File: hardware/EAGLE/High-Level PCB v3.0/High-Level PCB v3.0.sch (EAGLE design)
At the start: 38 parts, among them IC1 DS8921, IC2 DS8921, IC3 MCP2551, J1 Micro-SD, J2 Gyro, J3 Compass, J4 GPS, J5 DB9 Plug, J6 Compass, X1 RJ45, X2 Vehicle control, X4 RJ45

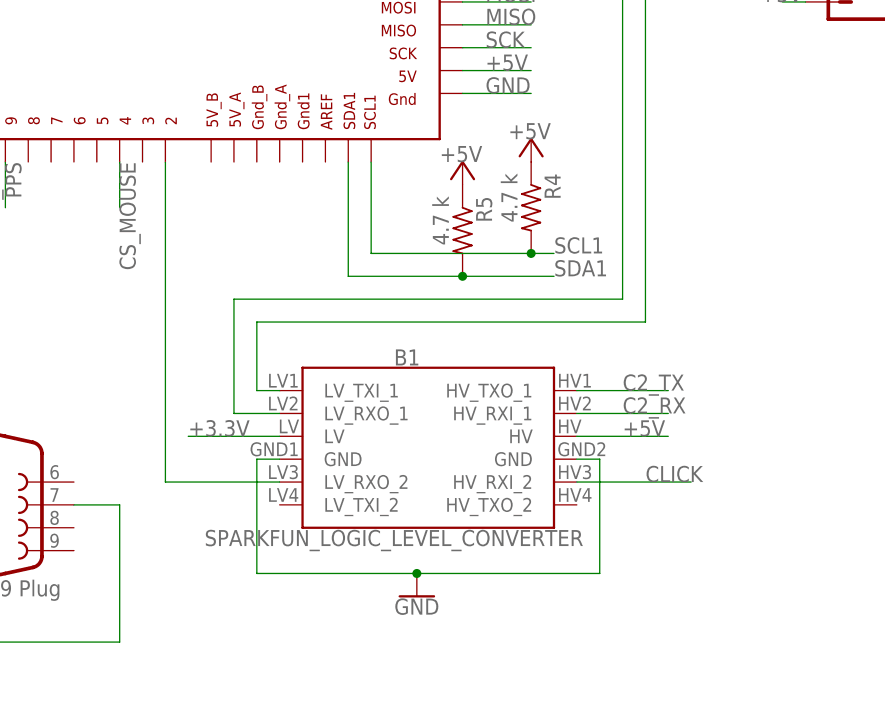
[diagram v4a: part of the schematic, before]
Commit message: Voltage level shifter adafruit
Removed Sparkfun voltage level shifter and replaced with adafruit's
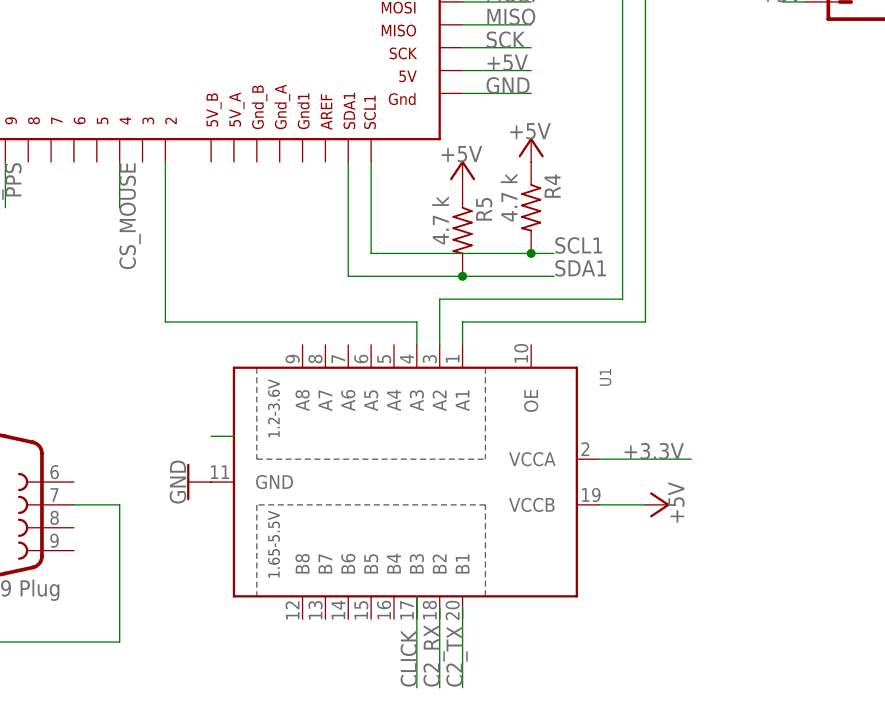
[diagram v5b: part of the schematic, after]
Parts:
- removed B1: SPARKFUN_LOGIC_LEVEL_CONVERTER, SparkFun-Boards:SPARKFUN_LOGIC_LEVEL_CONVERTER
- added U1: (no value), TXb0108:TXB0108PWR
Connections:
- net +3.3V: now also U1.VCCA; no longer B1.LV
- net +5V: now also U1.VCCB; no longer B1.HV
- net C2_RX: no longer B1.HV_RXI_1
- net C2_TX: no longer B1.HV_TXO_1
- net CLICK: no longer B1.HV_RXI_2
- net GND: now also U1.GND; no longer B1.GND, B1.GND@2
- net N$12: now also U1.A3; no longer B1.LV_RXO_2
- net N$4: now also U1.A1; no longer B1.LV_TXI_1
- net N$5: now also U1.A2; no longer B1.LV_RXO_1
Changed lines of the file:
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@@
 <part name="P+2" library="supply1" library_urn="urn:adsk.eagle:library:371" deviceset="+5V" device=""/>
 <part name="P+3" library="supply1" library_urn="urn:adsk.eagle:library:371" deviceset="+5V" device=""/>
-<part name="B1" library="SparkFun-Boards" deviceset="SPARKFUN_LOGIC_LEVEL_CONVERTER" device=""/>
 <part name="GND7" library="SparkFun-PowerSymbols" deviceset="GND" device=""/>
 <part name="S2" library="switch" library_urn="urn:adsk.eagle:library:380" deviceset="255SB" device="" package3d_urn="urn:adsk.eagle:package:27679/1" value="Click Source"/>
@@
 <part name="J7" library="SparkFun-Connectors" deviceset="CONN_03" device="-SCREW-5MM"/>
 <part name="GND11" library="SparkFun-PowerSymbols" deviceset="GND" device=""/>
+<part name="U1" library="TXb0108" deviceset="TXB0108PWR" device=""/>
+<part name="P+7" library="supply1" library_urn="urn:adsk.eagle:library:371" deviceset="+5V" device=""/>
 </parts>
 <sheets>
@@
 <instance part="P+2" gate="1" x="185.42" y="200.66"/>
 <instance part="P+3" gate="1" x="185.42" y="167.64"/>
-<instance part="B1" gate="G$1" x="139.7" y="27.94" smashed="yes">
-<attribute name="NAME" x="134.62" y="38.354" size="1.778" layer="95" font="vector"/>
-<attribute name="VALUE" x="134.62" y="20.066" size="1.778" layer="95" font="vector" align="top-center"/>
-</instance>
-<instance part="GND7" gate="1" x="137.16" y="12.7"/>
+<instance part="GND7" gate="1" x="111.76" y="25.4" rot="R270"/>
 <instance part="S2" gate="1" x="50.8" y="175.26"/>
 <instance part="JP2" gate="A" x="187.96" y="121.92" smashed="yes" rot="R90">
@@
 <instance part="J7" gate="J$1" x="12.7" y="17.78"/>
 <instance part="GND11" gate="1" x="22.86" y="10.16"/>
+<instance part="U1" gate="G$1" x="137.16" y="25.4" rot="R270"/>
+<instance part="P+7" gate="1" x="165.1" y="22.86" smashed="yes" rot="R270">
+<attribute name="VALUE" x="165.1" y="25.4" size="1.778" layer="96" rot="R270"/>
+</instance>
 </instances>
 <busses>
@@
 <pinref part="X1" gate="G$1" pin="1"/>
 <wire x1="243.84" y1="180.34" x2="251.46" y2="180.34" width="0.1524" layer="91"/>
-</segment>
-<segment>
-<pinref part="B1" gate="G$1" pin="GND"/>
-<wire x1="121.92" y1="27.94" x2="119.38" y2="27.94" width="0.1524" layer="91"/>
-<wire x1="119.38" y1="27.94" x2="119.38" y2="15.24" width="0.1524" layer="91"/>
-<wire x1="119.38" y1="15.24" x2="137.16" y2="15.24" width="0.1524" layer="91"/>
-<wire x1="137.16" y1="15.24" x2="157.48" y2="15.24" width="0.1524" layer="91"/>
-<wire x1="157.48" y1="15.24" x2="157.48" y2="27.94" width="0.1524" layer="91"/>
-<pinref part="B1" gate="G$1" pin="GND@2"/>
-<wire x1="157.48" y1="27.94" x2="154.94" y2="27.94" width="0.1524" layer="91"/>
-<pinref part="GND7" gate="1" pin="GND"/>
-<junction x="137.16" y="15.24"/>
 </segment>
 <segment>
@@
 <wire x1="22.86" y1="15.24" x2="22.86" y2="12.7" width="0.1524" layer="91"/>
 </segment>
+<segment>
+<pinref part="U1" gate="G$1" pin="GND"/>
+<pinref part="GND7" gate="1" pin="GND"/>
+</segment>
 </net>
 <net name="INT1" class="0">
@@
 <net name="CLICK" class="0">
 <segment>
-<pinref part="B1" gate="G$1" pin="HV_RXI_2"/>
-<wire x1="154.94" y1="25.4" x2="167.64" y2="25.4" width="0.1524" layer="91"/>
-<label x="162.56" y="25.4" size="1.778" layer="95"/>
-</segment>
-<segment>
 <pinref part="S2" gate="1" pin="P"/>
 <wire x1="53.34" y1="170.18" x2="53.34" y2="160.02" width="0.1524" layer="91"/>
 <wire x1="53.34" y1="160.02" x2="55.88" y2="160.02" width="0.1524" layer="91"/>
 <label x="55.88" y="160.02" size="1.778" layer="95"/>
+<label x="137.16" y="2.54" size="1.778" layer="95" rot="R90"/>
+</segment>
+<segment>
+<wire x1="137.16" y1="12.7" x2="137.16" y2="2.54" width="0.1524" layer="91"/>
 </segment>
 </net>
@@
 <wire x1="69.85" y1="187.96" x2="60.96" y2="187.96" width="0.1524" layer="91"/>
 <label x="60.96" y="187.96" size="1.778" layer="95"/>
-</segment>
-<segment>
-<pinref part="B1" gate="G$1" pin="HV_TXO_1"/>
-<wire x1="154.94" y1="35.56" x2="165.1" y2="35.56" width="0.1524" layer="91"/>
-<label x="160.02" y="35.56" size="1.778" layer="95"/>
+<label x="142.24" y="2.54" size="1.778" layer="95" rot="R90"/>
+</segment>
+<segment>
+<wire x1="142.24" y1="11.43" x2="142.24" y2="2.54" width="0.1524" layer="91"/>
 </segment>
 </net>
@@
 </segment>
 <segment>
-<pinref part="B1" gate="G$1" pin="HV"/>
-<wire x1="154.94" y1="30.48" x2="165.1" y2="30.48" width="0.1524" layer="91"/>
-<label x="160.02" y="30.48" size="1.778" layer="95"/>
-</segment>
-<segment>
 <pinref part="JP2" gate="A" pin="2"/>
 <wire x1="180.34" y1="121.92" x2="177.8" y2="121.92" width="0.1524" layer="91"/>
@@
 <wire x1="10.16" y1="48.26" x2="15.24" y2="48.26" width="0.1524" layer="91"/>
 </segment>
+<segment>
+<pinref part="P+7" gate="1" pin="+5V"/>
+<pinref part="U1" gate="G$1" pin="VCCB"/>
+<wire x1="162.56" y1="22.86" x2="157.48" y2="22.86" width="0.1524" layer="91"/>
+</segment>
 </net>
 <net name="CANRX" class="0">
@@
 <wire x1="142.24" y1="134.62" x2="152.4" y2="134.62" width="0.1524" layer="91"/>
 <label x="144.78" y="134.62" size="1.778" layer="95"/>
-</segment>
-<segment>
-<pinref part="B1" gate="G$1" pin="LV"/>
-<wire x1="121.92" y1="30.48" x2="111.76" y2="30.48" width="0.1524" layer="91"/>
-<label x="111.76" y="30.48" size="1.778" layer="95"/>
+<label x="160.02" y="27.94" size="1.778" layer="95"/>
+</segment>
+<segment>
+<wire x1="157.48" y1="27.94" x2="167.64" y2="27.94" width="0.1524" layer="91"/>
+<pinref part="U1" gate="G$1" pin="VCCA"/>
 </segment>
 </net>
 <net name="N$12" class="0">
 <segment>
-<pinref part="B1" gate="G$1" pin="LV_RXO_2"/>
-<wire x1="121.92" y1="25.4" x2="109.22" y2="25.4" width="0.1524" layer="91"/>
 <pinref part="U$1" gate="G$1" pin="2"/>
-<wire x1="109.22" y1="25.4" x2="109.22" y2="60.96" width="0.1524" layer="91"/>
+<pinref part="U1" gate="G$1" pin="A3"/>
+<wire x1="109.22" y1="43.18" x2="109.22" y2="60.96" width="0.1524" layer="91"/>
+<wire x1="137.16" y1="40.64" x2="137.16" y2="43.18" width="0.1524" layer="91"/>
+<wire x1="137.16" y1="43.18" x2="109.22" y2="43.18" width="0.1524" layer="91"/>
 </segment>
 </net>
@@
 <wire x1="69.85" y1="190.5" x2="60.96" y2="190.5" width="0.1524" layer="91"/>
 <label x="60.96" y="190.5" size="1.778" layer="95"/>
-</segment>
-<segment>
-<pinref part="B1" gate="G$1" pin="HV_RXI_1"/>
-<wire x1="154.94" y1="33.02" x2="165.1" y2="33.02" width="0.1524" layer="91"/>
-<label x="160.02" y="33.02" size="1.778" layer="95"/>
+<label x="139.7" y="2.54" size="1.778" layer="95" rot="R90"/>
+</segment>
+<segment>
+<wire x1="139.7" y1="11.43" x2="139.7" y2="2.54" width="0.1524" layer="91"/>
 </segment>
 </net>
 <net name="N$4" class="0">
 <segment>
-<pinref part="B1" gate="G$1" pin="LV_TXI_1"/>
-<wire x1="121.92" y1="35.56" x2="119.38" y2="35.56" width="0.1524" layer="91"/>
-<wire x1="119.38" y1="35.56" x2="119.38" y2="43.18" width="0.1524" layer="91"/>
-<wire x1="119.38" y1="43.18" x2="162.56" y2="43.18" width="0.1524" layer="91"/>
-<wire x1="162.56" y1="43.18" x2="162.56" y2="99.06" width="0.1524" layer="91"/>
 <pinref part="U$1" gate="G$1" pin="RX2"/>
 <wire x1="162.56" y1="99.06" x2="142.24" y2="99.06" width="0.1524" layer="91"/>
+<pinref part="U1" gate="G$1" pin="A1"/>
+<wire x1="142.24" y1="40.64" x2="142.24" y2="43.18" width="0.1524" layer="91"/>
+<wire x1="142.24" y1="43.18" x2="162.56" y2="43.18" width="0.1524" layer="91"/>
+<wire x1="162.56" y1="43.18" x2="162.56" y2="99.06" width="0.1524" layer="91"/>
 </segment>
 </net>
@@
 <wire x1="142.24" y1="96.52" x2="160.02" y2="96.52" width="0.1524" layer="91"/>
 <wire x1="160.02" y1="96.52" x2="160.02" y2="45.72" width="0.1524" layer="91"/>
-<wire x1="160.02" y1="45.72" x2="116.84" y2="45.72" width="0.1524" layer="91"/>
-<wire x1="116.84" y1="45.72" x2="116.84" y2="33.02" width="0.1524" layer="91"/>
-<pinref part="B1" gate="G$1" pin="LV_RXO_1"/>
-<wire x1="116.84" y1="33.02" x2="121.92" y2="33.02" width="0.1524" layer="91"/>
+<wire x1="160.02" y1="45.72" x2="139.7" y2="45.72" width="0.1524" layer="91"/>
+<pinref part="U1" gate="G$1" pin="A2"/>
+<wire x1="139.7" y1="45.72" x2="139.7" y2="40.64" width="0.1524" layer="91"/>
 </segment>
 </net>
@@
 </segment>
 </net>
+<net name="N$23" class="0">
+<segment>
+<wire x1="116.84" y1="30.48" x2="114.3" y2="30.48" width="0.1524" layer="91"/>
+</segment>
+</net>

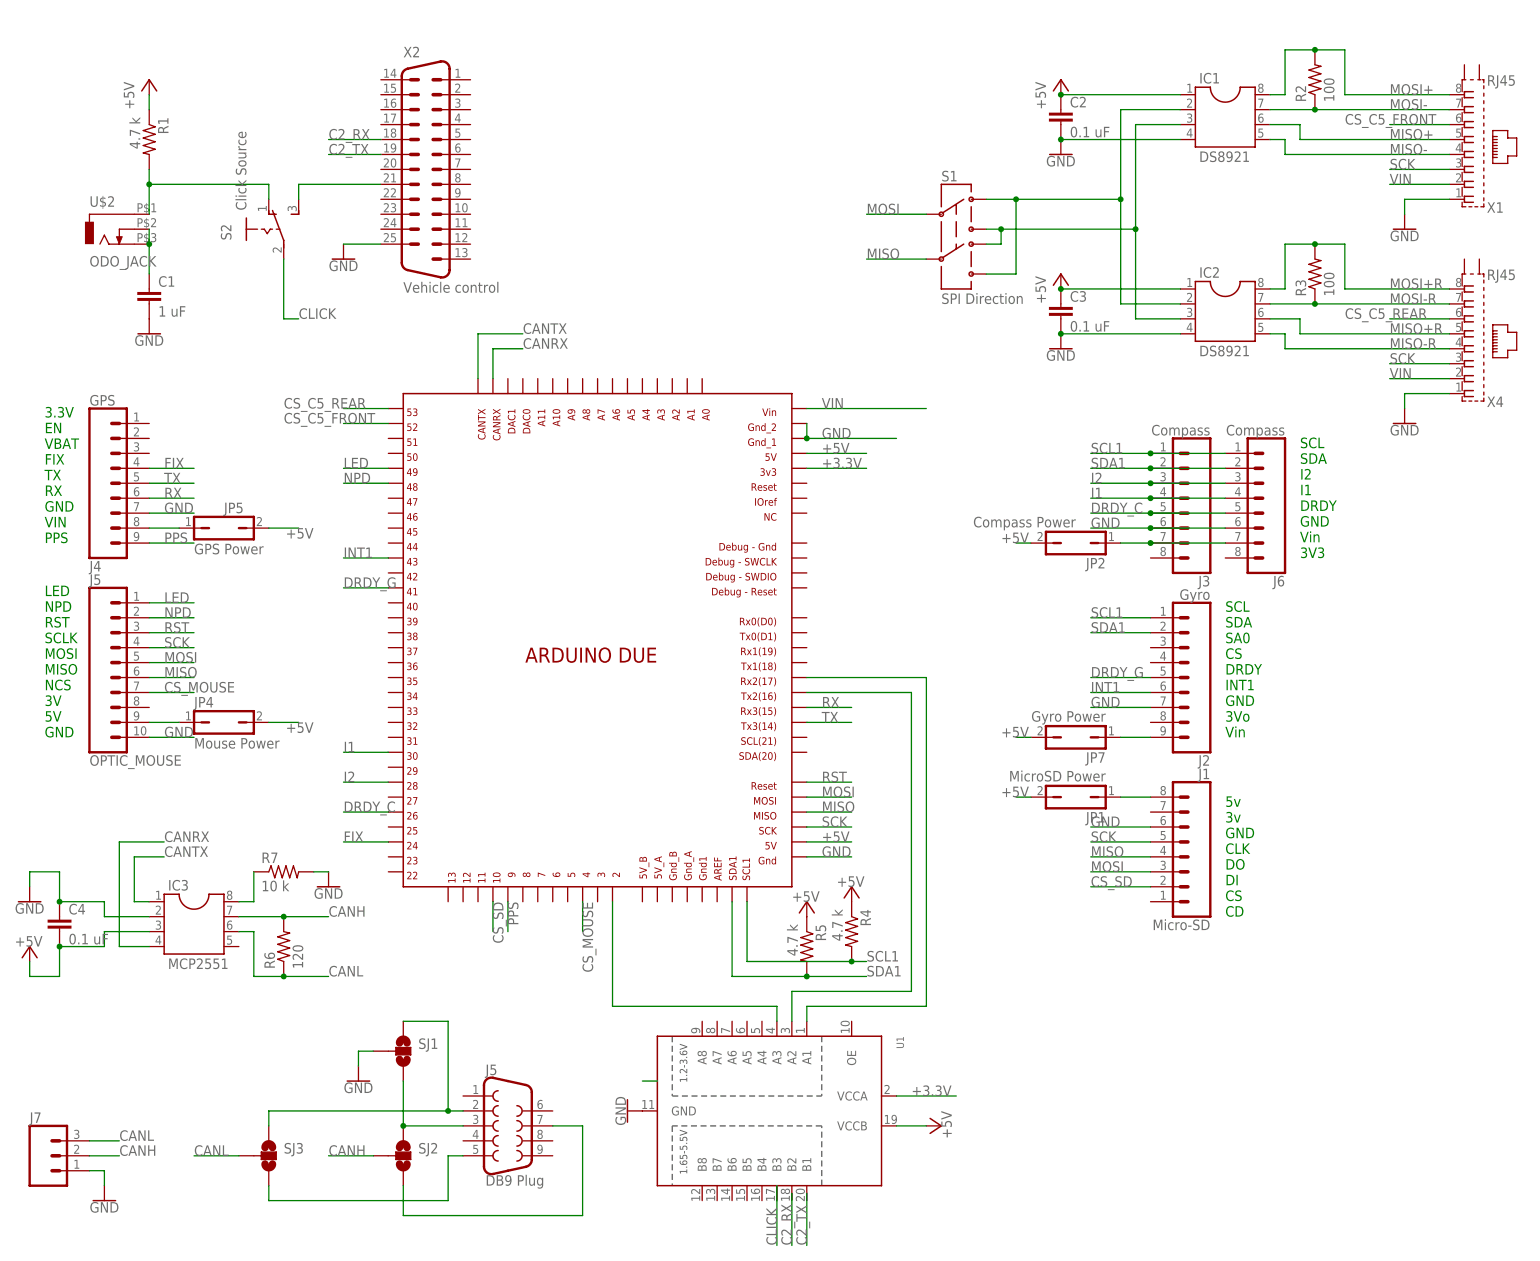
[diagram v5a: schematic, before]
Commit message: Moved some stuff around and re-routed the logic converter chip
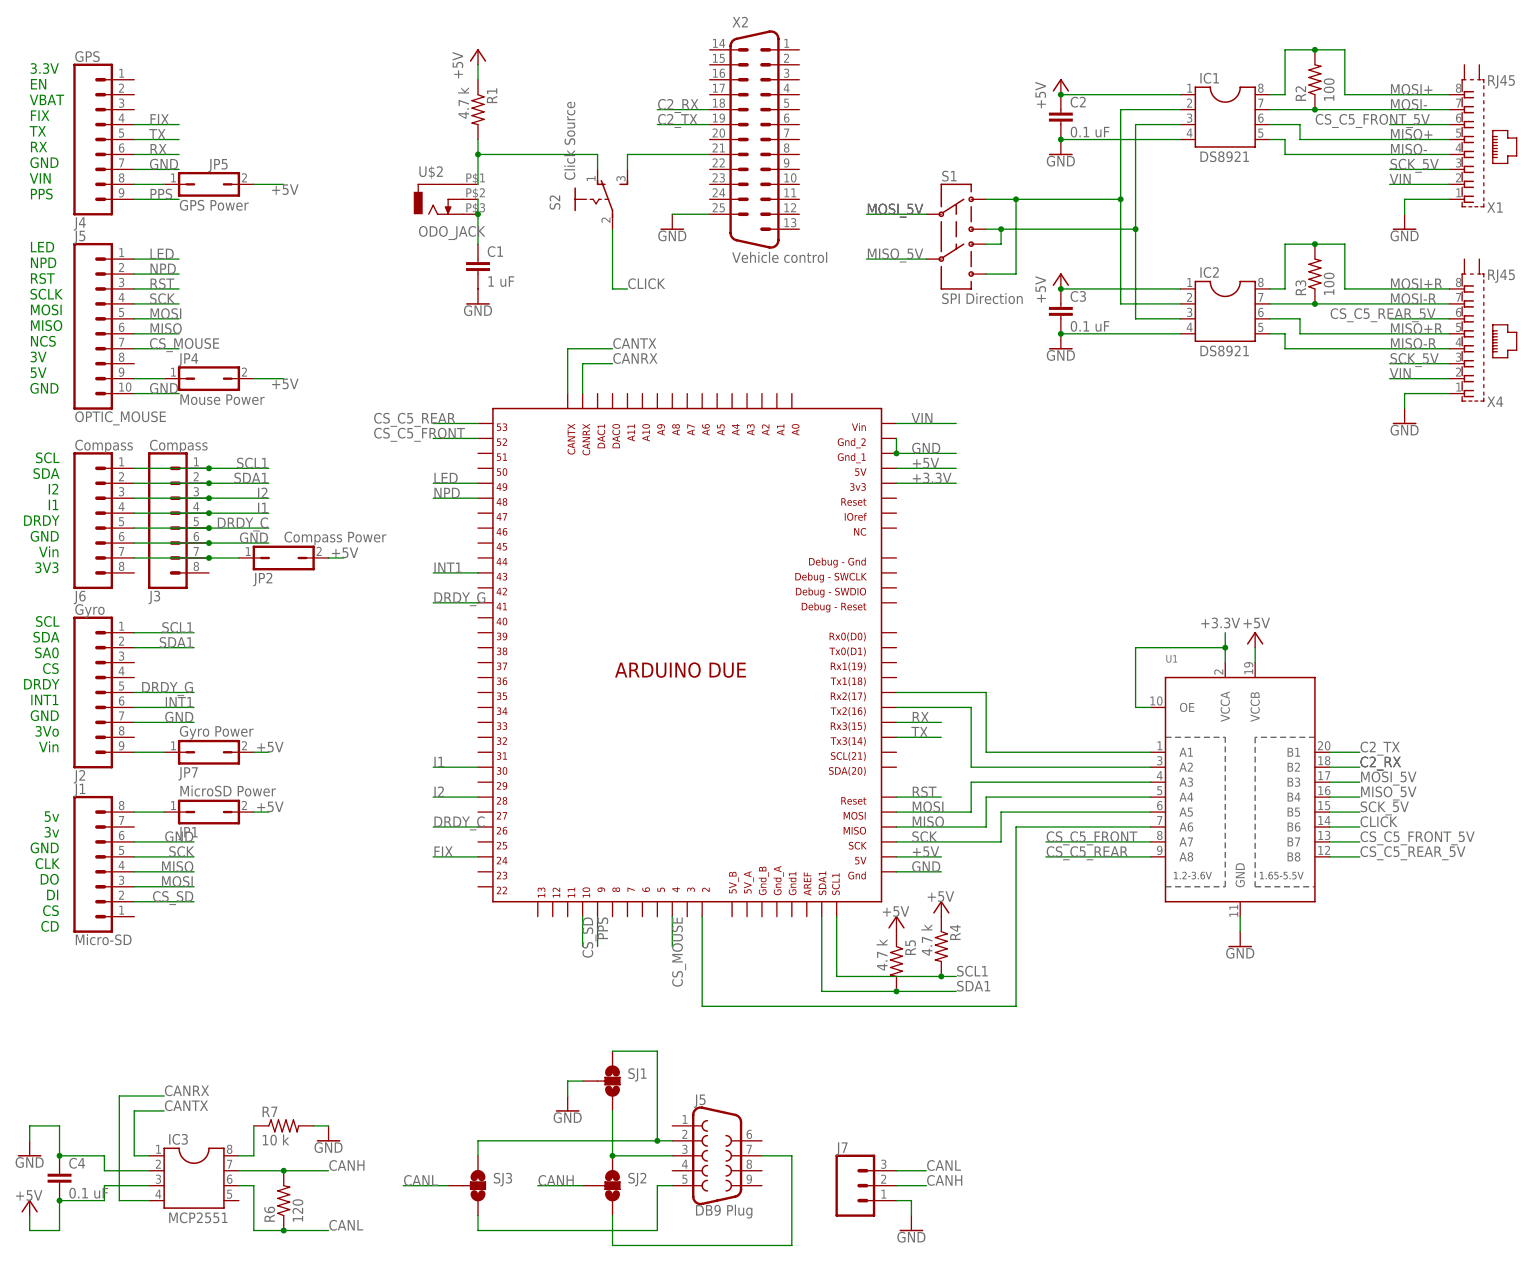
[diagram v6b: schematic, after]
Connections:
- new net CS_C5_FRONT_5V: U1.B7, X1.6
- new net CS_C5_REAR_5V: U1.B8, X4.6
- new net MISO_5V: S1.5, U1.B4
- new net MOSI_5V: S1.2, U1.B3
- new net SCK_5V: U1.B5, X1.3, X4.3
- net +3.3V: now also U1.OE
- net C2_RX: now also U1.B2
- net C2_TX: now also U1.B1
- net CLICK: now also U1.B6
- net CS_C5_FRONT: now also U1.A7; no longer X1.6
- net CS_C5_REAR: now also U1.A8; no longer X4.6
- net MISO: now also U1.A4; no longer S1.5
- net MOSI: now also U1.A3; no longer S1.2
- net N$12: now also U1.A6; no longer U1.A3
- net SCK: now also U1.A5; no longer X1.3, X4.3
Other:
- moved on the sheet: C1, C4, IC3, J1, J2, J3, J4, J5, J6, J7, JP1, JP2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
